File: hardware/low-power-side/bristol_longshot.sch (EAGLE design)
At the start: 70 parts, among them U1 SAM_D20E, U10 ADP1607ACPZN-R7, U11 TPS73118DBVT, U2 SI4060, U3 SE880, U4 SST25WF040BT-40I/NP, U5 TG-5006CJ, U6 TG-5006CJ, U7 TPS3123, U8 SN74LVC1G32DCKR, U9 MS5607-02BA03, Y1 ABS05

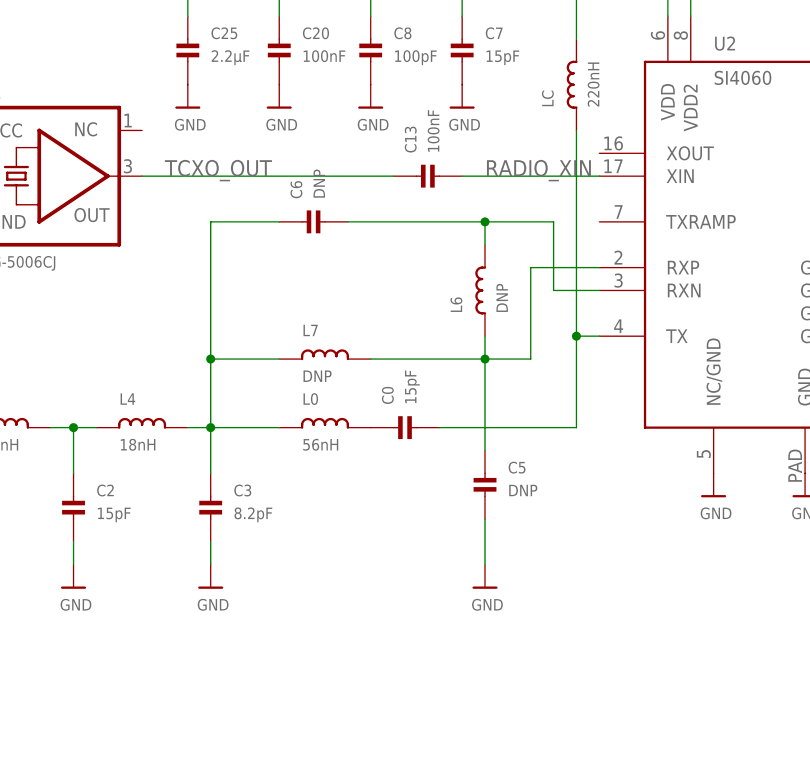
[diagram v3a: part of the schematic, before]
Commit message: Low Power. Added L0'-C0' tank in paralell. Might work, should test
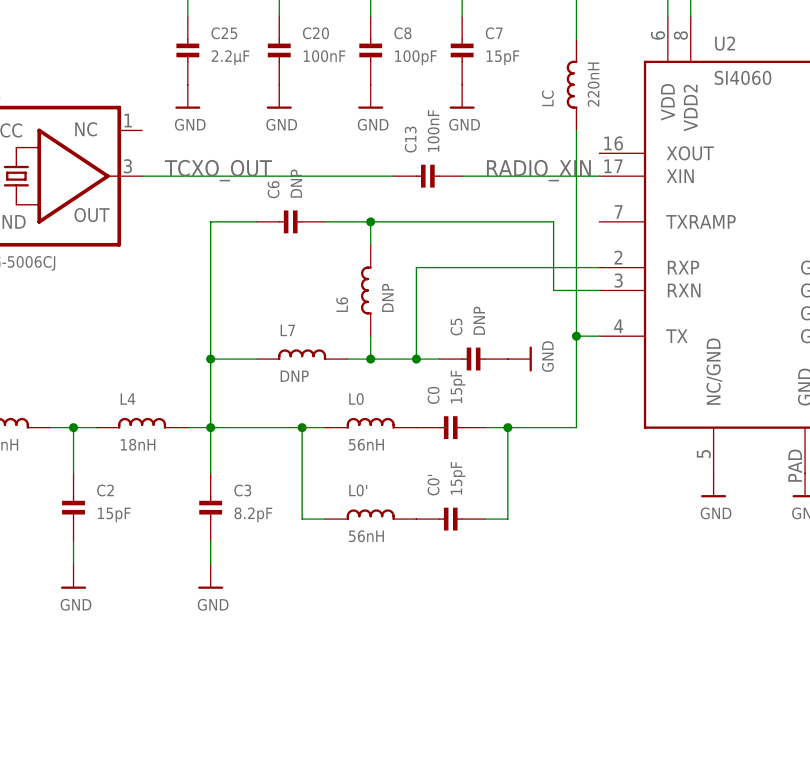
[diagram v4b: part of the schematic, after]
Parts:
- added C0': 15pF, microbuilder_v3:CAP_CERAMIC_0402
- added L0': 56nH, microbuilder_v3:INDUCTOR_0402
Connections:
- new net N$5: C0'.P$1, L0'.2
- net FILTER1: now also L0'.1
- net RF_OUT: now also C0'.P$2
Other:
- moved on the sheet: C0, C5, C6, L0, L6, L7
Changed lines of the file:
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@@
 <part name="U$48" library="microbuilder_v3" deviceset="1.8V" device=""/>
 <part name="U$54" library="microbuilder_v3" deviceset="1.8V" device=""/>
+<part name="L0'" library="microbuilder_v3" deviceset="INDUCTOR" device="_0402" value="56nH"/>
+<part name="C0'" library="microbuilder_v3" deviceset="CAP_CERAMIC" device="_0402" value="15pF"/>
 </parts>
 <sheets>
@@
 <instance part="LC" gate="G$1" x="594.36" y="205.74" rot="R90"/>
 <instance part="FB1" gate="G$1" x="604.52" y="220.98" rot="R90"/>
-<instance part="C0" gate="G$1" x="576.58" y="167.64" rot="R90"/>
-<instance part="L0" gate="G$1" x="566.42" y="167.64"/>
+<instance part="C0" gate="G$1" x="581.66" y="167.64" rot="R90"/>
+<instance part="L0" gate="G$1" x="571.5" y="167.64"/>
 <instance part="C3" gate="G$1" x="553.72" y="157.48"/>
 <instance part="L4" gate="G$1" x="546.1" y="167.64"/>
@@
 <instance part="C9" gate="G$1" x="462.28" y="96.52"/>
 <instance part="U$3" gate="G$1" x="462.28" y="88.9"/>
-<instance part="L6" gate="G$1" x="584.2" y="182.88" rot="R90"/>
-<instance part="C5" gate="G$1" x="584.2" y="160.02"/>
-<instance part="U$45" gate="G$1" x="584.2" y="149.86"/>
-<instance part="L7" gate="G$1" x="566.42" y="175.26"/>
-<instance part="C6" gate="G$1" x="566.42" y="190.5" rot="R90"/>
+<instance part="L6" gate="G$1" x="571.5" y="182.88" rot="R90"/>
+<instance part="C5" gate="G$1" x="584.2" y="175.26" rot="R90"/>
+<instance part="U$45" gate="G$1" x="589.28" y="175.26" rot="R90"/>
+<instance part="L7" gate="G$1" x="563.88" y="175.26"/>
+<instance part="C6" gate="G$1" x="563.88" y="190.5" rot="R90"/>
 <instance part="C14" gate="G$1" x="452.12" y="96.52"/>
 <instance part="U$18" gate="G$1" x="452.12" y="88.9"/>
@@
 <instance part="U$48" gate="G$1" x="256.54" y="53.34" rot="MR0"/>
 <instance part="U$54" gate="G$1" x="266.7" y="53.34" rot="MR0"/>
+<instance part="L0'" gate="G$1" x="571.5" y="157.48"/>
+<instance part="C0'" gate="G$1" x="581.66" y="157.48" rot="R90"/>
 </instances>
 <busses>
@@
 <pinref part="U$45" gate="G$1" pin="GND"/>
 <pinref part="C5" gate="G$1" pin="P$2"/>
-<wire x1="584.2" y1="152.4" x2="584.2" y2="157.48" width="0.1524" layer="91"/>
 </segment>
 <segment>
@@
 <pinref part="C0" gate="G$1" pin="P$2"/>
 <wire x1="594.36" y1="177.8" x2="594.36" y2="167.64" width="0.1524" layer="91"/>
-<wire x1="594.36" y1="167.64" x2="579.12" y2="167.64" width="0.1524" layer="91"/>
+<wire x1="594.36" y1="167.64" x2="586.74" y2="167.64" width="0.1524" layer="91"/>
 <pinref part="U2" gate="G$1" pin="TX"/>
+<wire x1="586.74" y1="167.64" x2="584.2" y2="167.64" width="0.1524" layer="91"/>
 <wire x1="596.9" y1="177.8" x2="594.36" y2="177.8" width="0.1524" layer="91"/>
 <junction x="594.36" y="177.8"/>
+<pinref part="C0'" gate="G$1" pin="P$2"/>
+<wire x1="584.2" y1="157.48" x2="586.74" y2="157.48" width="0.1524" layer="91"/>
+<wire x1="586.74" y1="157.48" x2="586.74" y2="167.64" width="0.1524" layer="91"/>
+<junction x="586.74" y="167.64"/>
 </segment>
 </net>
@@
 <pinref part="L0" gate="G$1" pin="1"/>
 <pinref part="L4" gate="G$1" pin="2"/>
-<wire x1="561.34" y1="167.64" x2="553.72" y2="167.64" width="0.1524" layer="91"/>
+<wire x1="566.42" y1="167.64" x2="563.88" y2="167.64" width="0.1524" layer="91"/>
 <pinref part="C3" gate="G$1" pin="P$1"/>
+<wire x1="563.88" y1="167.64" x2="553.72" y2="167.64" width="0.1524" layer="91"/>
 <wire x1="553.72" y1="167.64" x2="551.18" y2="167.64" width="0.1524" layer="91"/>
 <wire x1="553.72" y1="167.64" x2="553.72" y2="162.56" width="0.1524" layer="91"/>
 <junction x="553.72" y="167.64"/>
 <pinref part="L7" gate="G$1" pin="1"/>
-<wire x1="561.34" y1="175.26" x2="553.72" y2="175.26" width="0.1524" layer="91"/>
+<wire x1="558.8" y1="175.26" x2="553.72" y2="175.26" width="0.1524" layer="91"/>
 <wire x1="553.72" y1="175.26" x2="553.72" y2="167.64" width="0.1524" layer="91"/>
 <pinref part="C6" gate="G$1" pin="P$1"/>
-<wire x1="561.34" y1="190.5" x2="553.72" y2="190.5" width="0.1524" layer="91"/>
+<wire x1="558.8" y1="190.5" x2="553.72" y2="190.5" width="0.1524" layer="91"/>
 <wire x1="553.72" y1="190.5" x2="553.72" y2="175.26" width="0.1524" layer="91"/>
 <junction x="553.72" y="175.26"/>
+<pinref part="L0'" gate="G$1" pin="1"/>
+<wire x1="566.42" y1="157.48" x2="563.88" y2="157.48" width="0.1524" layer="91"/>
+<wire x1="563.88" y1="157.48" x2="563.88" y2="167.64" width="0.1524" layer="91"/>
+<junction x="563.88" y="167.64"/>
 </segment>
 </net>
@@
 <wire x1="591.82" y1="182.88" x2="591.82" y2="190.5" width="0.1524" layer="91"/>
 <pinref part="L6" gate="G$1" pin="2"/>
-<wire x1="591.82" y1="190.5" x2="584.2" y2="190.5" width="0.1524" layer="91"/>
-<wire x1="584.2" y1="190.5" x2="584.2" y2="187.96" width="0.1524" layer="91"/>
+<wire x1="591.82" y1="190.5" x2="571.5" y2="190.5" width="0.1524" layer="91"/>
+<wire x1="571.5" y1="190.5" x2="571.5" y2="187.96" width="0.1524" layer="91"/>
 <pinref part="C6" gate="G$1" pin="P$2"/>
-<wire x1="568.96" y1="190.5" x2="584.2" y2="190.5" width="0.1524" layer="91"/>
-<junction x="584.2" y="190.5"/>
+<wire x1="566.42" y1="190.5" x2="571.5" y2="190.5" width="0.1524" layer="91"/>
+<junction x="571.5" y="190.5"/>
 <pinref part="U2" gate="G$1" pin="RXN"/>
 <wire x1="591.82" y1="182.88" x2="596.9" y2="182.88" width="0.1524" layer="91"/>
@@
 <net name="RXN" class="0">
 <segment>
-<wire x1="589.28" y1="185.42" x2="589.28" y2="175.26" width="0.1524" layer="91"/>
+<wire x1="576.58" y1="185.42" x2="576.58" y2="175.26" width="0.1524" layer="91"/>
 <pinref part="L6" gate="G$1" pin="1"/>
-<wire x1="589.28" y1="175.26" x2="584.2" y2="175.26" width="0.1524" layer="91"/>
-<wire x1="584.2" y1="175.26" x2="584.2" y2="177.8" width="0.1524" layer="91"/>
-<junction x="584.2" y="175.26"/>
+<wire x1="571.5" y1="175.26" x2="571.5" y2="177.8" width="0.1524" layer="91"/>
+<junction x="571.5" y="175.26"/>
 <pinref part="L7" gate="G$1" pin="2"/>
-<wire x1="571.5" y1="175.26" x2="584.2" y2="175.26" width="0.1524" layer="91"/>
+<wire x1="568.96" y1="175.26" x2="571.5" y2="175.26" width="0.1524" layer="91"/>
 <pinref part="C5" gate="G$1" pin="P$1"/>
-<wire x1="584.2" y1="175.26" x2="584.2" y2="165.1" width="0.1524" layer="91"/>
+<wire x1="571.5" y1="175.26" x2="576.58" y2="175.26" width="0.1524" layer="91"/>
 <pinref part="U2" gate="G$1" pin="RXP"/>
-<wire x1="596.9" y1="185.42" x2="589.28" y2="185.42" width="0.1524" layer="91"/>
+<wire x1="576.58" y1="175.26" x2="579.12" y2="175.26" width="0.1524" layer="91"/>
+<wire x1="596.9" y1="185.42" x2="576.58" y2="185.42" width="0.1524" layer="91"/>
+<junction x="576.58" y="175.26"/>
 </segment>
 </net>
@@
 </segment>
 </net>
+<net name="N$5" class="0">
+<segment>
+<pinref part="L0'" gate="G$1" pin="2"/>
+<pinref part="C0'" gate="G$1" pin="P$1"/>
+</segment>
+</net>

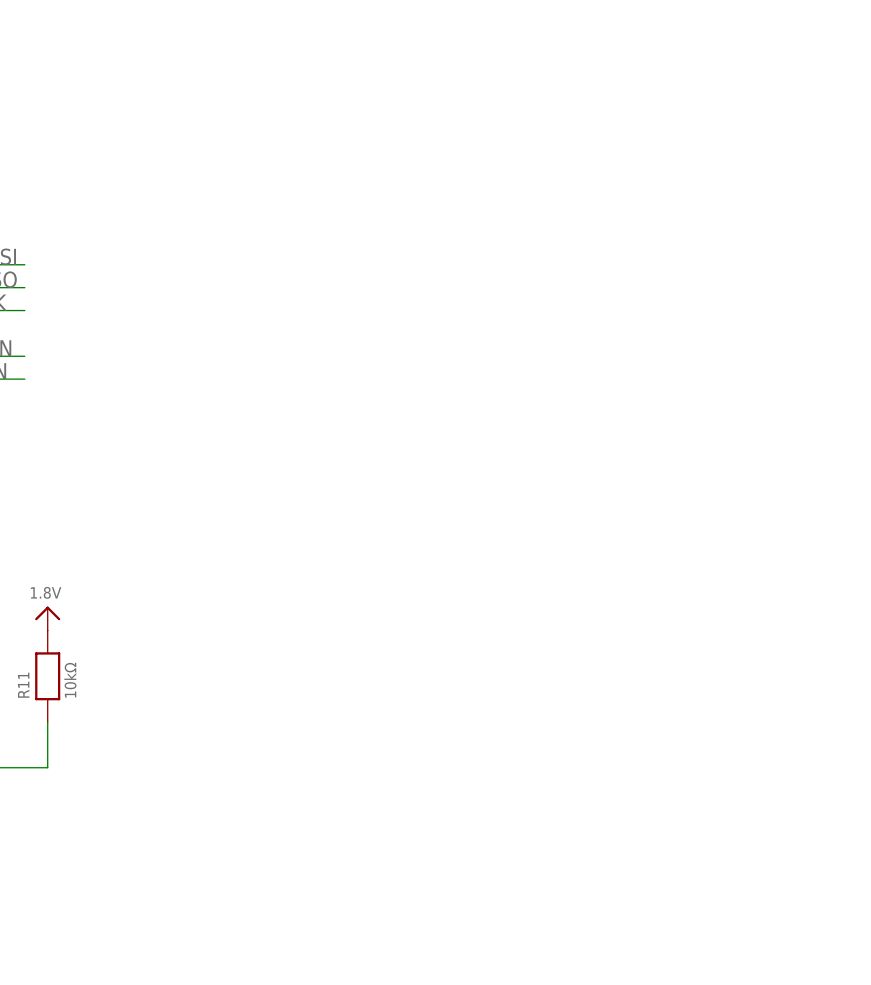
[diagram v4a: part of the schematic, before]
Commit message: low-power-side v0.986.4. Added LIS2D accelerometer. Optional
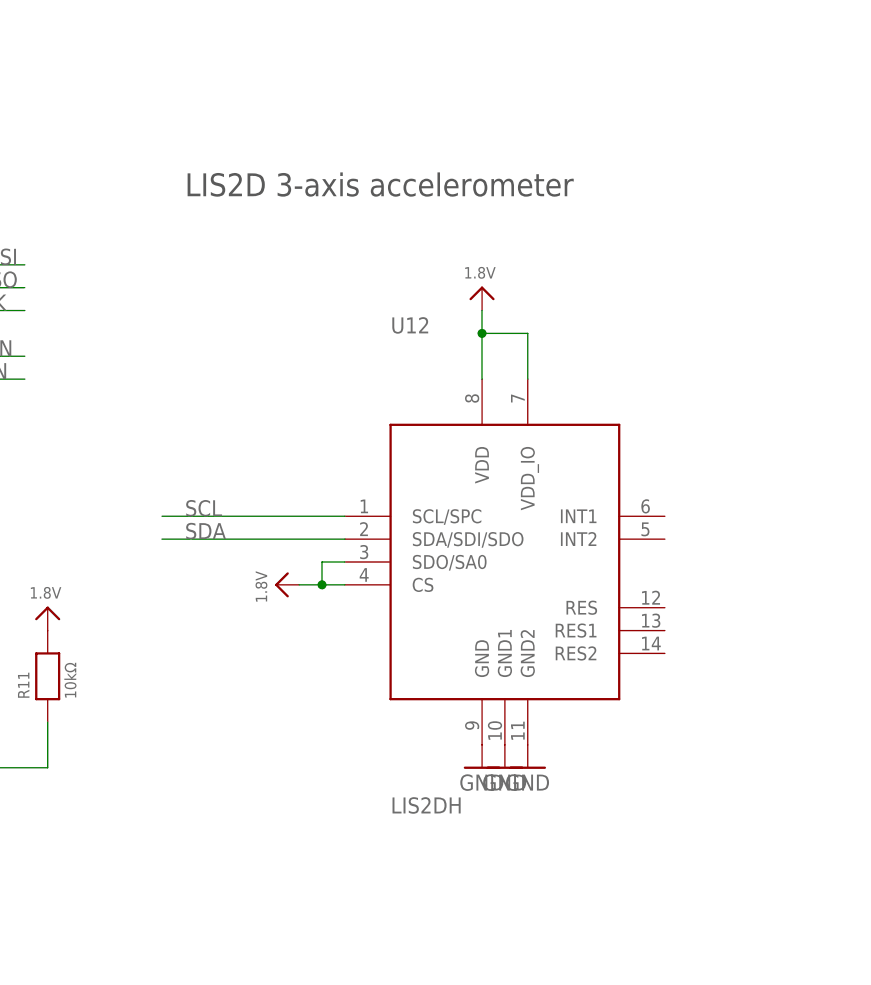
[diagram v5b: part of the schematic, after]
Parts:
- added U12: LIS2DH, fbri:LIS2DH
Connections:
- net 1.8V: now also U12.CS, U12.SDO/SA0, U12.VDD, U12.VDD_IO
- net GND: now also U12.GND, U12.GND1, U12.GND2
- net SCL: now also U12.SCL/SPC
- net SDA: now also U12.SDA/SDI/SDO
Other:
- note added: "LIS2D 3-axis accelerometer"
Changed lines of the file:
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@@
 <part name="L0'" library="microbuilder_v3" deviceset="INDUCTOR" device="_0402" value="56nH"/>
 <part name="C0'" library="microbuilder_v3" deviceset="CAP_CERAMIC" device="_0402" value="15pF"/>
+<part name="U12" library="fbri" deviceset="LIS2DH" device=""/>
+<part name="GND3" library="SparkFun" deviceset="GND" device=""/>
+<part name="GND4" library="SparkFun" deviceset="GND" device=""/>
+<part name="GND5" library="SparkFun" deviceset="GND" device=""/>
+<part name="U$66" library="microbuilder_v3" deviceset="1.8V" device=""/>
+<part name="U$69" library="microbuilder_v3" deviceset="1.8V" device=""/>
 </parts>
 <sheets>
@@
 the variablity is in V_FB
 Specified 1.76V - 1.85V</text>
+<text x="281.94" y="99.06" size="2.54" layer="97" font="vector" ratio="11">LIS2D 3-axis accelerometer</text>
 </plain>
 <instances>
@@
 <instance part="L0'" gate="G$1" x="571.5" y="157.48"/>
 <instance part="C0'" gate="G$1" x="581.66" y="157.48" rot="R90"/>
+<instance part="U12" gate="G$1" x="317.5" y="58.42"/>
+<instance part="GND3" gate="1" x="314.96" y="35.56"/>
+<instance part="GND4" gate="1" x="317.5" y="35.56"/>
+<instance part="GND5" gate="1" x="320.04" y="35.56"/>
+<instance part="U$66" gate="G$1" x="314.96" y="88.9" rot="MR0"/>
+<instance part="U$69" gate="G$1" x="292.1" y="55.88" rot="MR270"/>
 </instances>
 <busses>
@@
 <pinref part="R7" gate="G$1" pin="1"/>
 <pinref part="U$47" gate="G$1" pin="GND"/>
+</segment>
+<segment>
+<pinref part="U12" gate="G$1" pin="GND"/>
+<pinref part="GND3" gate="1" pin="GND"/>
+</segment>
+<segment>
+<pinref part="U12" gate="G$1" pin="GND1"/>
+<pinref part="GND4" gate="1" pin="GND"/>
+</segment>
+<segment>
+<pinref part="U12" gate="G$1" pin="GND2"/>
+<pinref part="GND5" gate="1" pin="GND"/>
 </segment>
 </net>
@@
 <pinref part="R11" gate="G$1" pin="2"/>
 <pinref part="U$54" gate="G$1" pin="1.8V"/>
+</segment>
+<segment>
+<pinref part="U12" gate="G$1" pin="VDD"/>
+<pinref part="U$66" gate="G$1" pin="1.8V"/>
+<wire x1="314.96" y1="78.74" x2="314.96" y2="83.82" width="0.1524" layer="91"/>
+<pinref part="U12" gate="G$1" pin="VDD_IO"/>
+<wire x1="314.96" y1="83.82" x2="314.96" y2="86.36" width="0.1524" layer="91"/>
+<wire x1="320.04" y1="78.74" x2="320.04" y2="83.82" width="0.1524" layer="91"/>
+<wire x1="320.04" y1="83.82" x2="314.96" y2="83.82" width="0.1524" layer="91"/>
+<junction x="314.96" y="83.82"/>
+</segment>
+<segment>
+<pinref part="U12" gate="G$1" pin="CS"/>
+<wire x1="299.72" y1="55.88" x2="297.18" y2="55.88" width="0.1524" layer="91"/>
+<pinref part="U$69" gate="G$1" pin="1.8V"/>
+<pinref part="U12" gate="G$1" pin="SDO/SA0"/>
+<wire x1="297.18" y1="55.88" x2="294.64" y2="55.88" width="0.1524" layer="91"/>
+<wire x1="299.72" y1="58.42" x2="297.18" y2="58.42" width="0.1524" layer="91"/>
+<wire x1="297.18" y1="58.42" x2="297.18" y2="55.88" width="0.1524" layer="91"/>
+<junction x="297.18" y="55.88"/>
 </segment>
 </net>
@@
 <wire x1="256.54" y1="38.1" x2="256.54" y2="40.64" width="0.1524" layer="91"/>
 </segment>
+<segment>
+<pinref part="U12" gate="G$1" pin="SDA/SDI/SDO"/>
+<wire x1="299.72" y1="60.96" x2="279.4" y2="60.96" width="0.1524" layer="91"/>
+<label x="281.94" y="60.96" size="1.778" layer="95"/>
+</segment>
 </net>
 <net name="SCL" class="0">
@@
 <wire x1="266.7" y1="35.56" x2="266.7" y2="40.64" width="0.1524" layer="91"/>
 </segment>
-</net>
+<segment>
+<pinref part="U12" gate="G$1" pin="SCL/SPC"/>
+<wire x1="299.72" y1="63.5" x2="279.4" y2="63.5" width="0.1524" layer="91"/>
+<label x="281.94" y="63.5" size="1.778" layer="95"/>
+</segment>
+</net>
